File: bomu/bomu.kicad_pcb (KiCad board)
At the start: 2 copper layers, 29 parts, among them U1 NRF52840-CKAA-R7

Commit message: Current work on the PCB
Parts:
- removed TP1, TP2: TestPoint, TestPoint:TestPoint_Pad_D1.0mm
- ANT1, C1, C10, C11, C12, C13, C14, C15, C2, C3, C4, C5, C6, C7, C8, C9, L1, L2, R1, U1, XTAL1, XTAL2: moved to B.Cu
- moved C8 19.2 mm to (134.5, 133.7), turned to 90 degrees
- moved C13 18.3 mm to (133.1, 139.5), turned to 180 degrees
- moved C12 17.1 mm to (133.1, 133.7)
- moved R1 17.0 mm to (133.1, 140.3), turned to 180 degrees
- moved C15 15.9 mm to (138.9, 139.0), turned to 180 degrees
- moved C11 15.4 mm to (137.3, 133.7), turned to 270 degrees
- moved C9 14.9 mm to (135.2, 133.7), turned to 90 degrees
- moved C7 14.6 mm to (133.1, 134.4)
- moved C10 13.7 mm to (135.9, 133.7), turned to 90 degrees
- moved TP6 12.6 mm to (141.5, 133.7), turned to 90 degrees
- moved C1 12.4 mm to (142.2, 139.8), turned to 270 degrees
- moved C5 11.2 mm to (138.9, 134.8), turned to 180 degrees
- moved C6 11.1 mm to (133.1, 138.1), turned to 180 degrees
- moved L2 11.0 mm to (142.9, 139.4), turned to 180 degrees
- moved C14 10.8 mm to (137.5, 139.0)
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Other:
- board outline added: 13 x 9.4 mm
- net class Default: clearance 0.2 -> 0.0762; trace_width 0.25 -> 0.0762
- rule trace_clearance: 0.2 -> 0.0762
- rule trace_min: 0.2 -> 0.0762
- rule via_min_drill: 0.3 -> 0.2

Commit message: Changing from 2-lyaer to 4-layer
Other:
- copper layers 2 -> 4
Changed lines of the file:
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@@
 (kicad_pcb (version 20171130) (host pcbnew "(5.1.8-0-10_14)")
   (general
-    (thickness 1.6)
+    (thickness 0.8)
     (drawings 95)
     (tracks 0)
@@
   (page A4)
   (layers
-    (0 F.Cu signal)
-    (31 B.Cu signal)
+    (0 F.Cu mixed)
+    (1 In1.Cu power)
+    (2 In2.Cu power)
+    (31 B.Cu mixed)
     (32 B.Adhes user)
     (33 F.Adhes user)
@@
     (38 B.Mask user)
     (39 F.Mask user)
-    (40 Dwgs.User user hide)
+    (40 Dwgs.User user)
     (41 Cmts.User user)
     (42 Eco1.User user)

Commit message: Updating footprints. Adding SWD pads
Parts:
- added TP1: TestPoint, TestPoint:TestPoint_Pad_D1.0mm, F.Cu at (144.2, 133.9)
- moved TP3 7.87 mm to (144.2, 132.9)
- moved C1 1.18 mm to (141.1, 140.3)
- moved L1 1.18 mm to (140.4, 140.0)
- moved L2 1.18 mm to (141.8, 140.0)
- moved TP5 1.02 mm to (143.5, 132.9)
- moved TP6 0.89 mm to (141.3, 132.9)
- moved TP4 0.41 mm to (142.4, 132.9)
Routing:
- net GND: track 0.00 -> 8.57 mm, vias 0 -> 1
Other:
- copper layers 4 -> 6

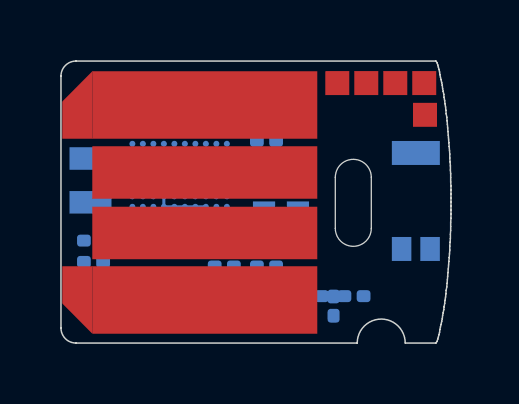
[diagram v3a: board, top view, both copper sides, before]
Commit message: Adjusting pour around antenna footprint. Adding more traces
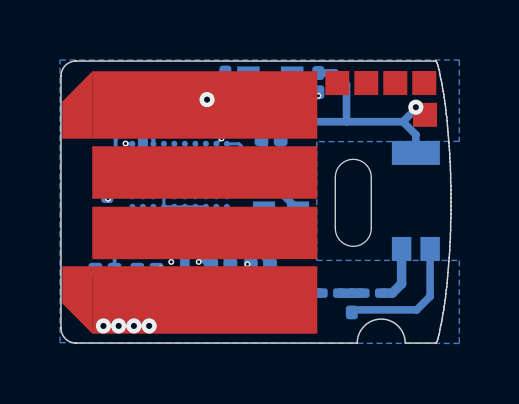
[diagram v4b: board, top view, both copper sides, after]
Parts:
- moved C6 9.16 mm to (140.6, 132.9), turned to 90 degrees
- moved XTAL2 6.75 mm to (139.0, 133.0), turned to 180 degrees
- moved C7 4.67 mm to (137.5, 132.8), turned to 270 degrees
- moved C12 2.63 mm to (133.6, 136.3), turned to 270 degrees
- moved C3 1.79 mm to (134.9, 139.1), turned to 0 degrees
- moved C15 1.53 mm to (137.4, 138.9), turned to 0 degrees
- moved C14 1.21 mm to (138.7, 138.9)
- moved C11 0.94 mm to (136.4, 133.7)
- moved C1 0.62 mm to (141.8, 140.2)
- moved L1 0.62 mm to (141.0, 139.9)
- moved L2 0.62 mm to (142.4, 139.9)
- moved C13 0.61 mm to (133.5, 139.1)
- moved C9 0.23 mm to (135.0, 133.7)
- moved C8 0.23 mm to (134.2, 133.7)
- moved C10 0.23 mm to (135.7, 133.7)
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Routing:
- net GND: track 8.57 -> 51.0 mm, vias 1 -> 9
- net +3V0: track 0.00 -> 18.5 mm, vias 0 -> 6
- net +5V: track 0.00 -> 12.1 mm, vias 0 -> 2
- net /ANT: track 0.00 -> 6.33 mm
- net /XL1: track 0.00 -> 5.83 mm, vias 0 -> 2
- net VBUS: track 0.00 -> 4.48 mm, vias 0 -> 4
- net /XL2: track 0.00 -> 2.69 mm, vias 0 -> 2
- net Net-(ANT1-PadFEED): track 0.00 -> 1.95 mm
- net Net-(C2-Pad1): track 0.00 -> 1.90 mm, vias 0 -> 2
- net Net-(C8-Pad1): track 0.00 -> 1.81 mm
- net Net-(C15-Pad2): track 0.00 -> 1.56 mm
- net Net-(C5-Pad1): track 0.00 -> 1.28 mm
- net Net-(C4-Pad2): track 0.00 -> 1.27 mm
- net Net-(C1-Pad1): track 0.00 -> 0.76 mm
- net (no net): vias 0 -> 19
- added copper zone on B.Cu, net GND

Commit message: Current work on ground planes
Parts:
- moved XTAL1 0.10 mm to (139.5, 136.5)
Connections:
- net /XL1 renamed /32XTAL_P
- net /XL2 renamed /32XTAL_N
- net Net-(C4-Pad2) renamed /XTAL_P
- net Net-(C5-Pad1) renamed /XTAL_N
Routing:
- net +3V0: track 18.5 -> 28.7 mm, vias 6 -> 7
- net /XTAL_P: track 1.27 -> 5.14 mm
- net /XTAL_N: track 1.28 -> 5.09 mm
- net /32XTAL_N: track 2.69 -> 5.15 mm
- net GND: track 51.0 -> 48.9 mm, vias 9 -> 48
- net /SWDCLK: vias 0 -> 1
- net (no net): vias 19 -> 2
- added copper zone on In4.Cu.GND, net GND

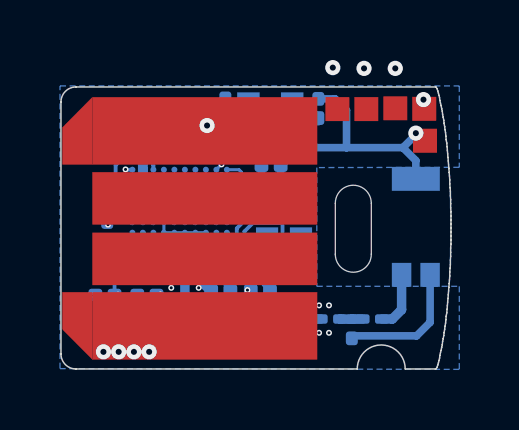
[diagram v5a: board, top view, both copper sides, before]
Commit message: Adding ground plane stitching with microvias
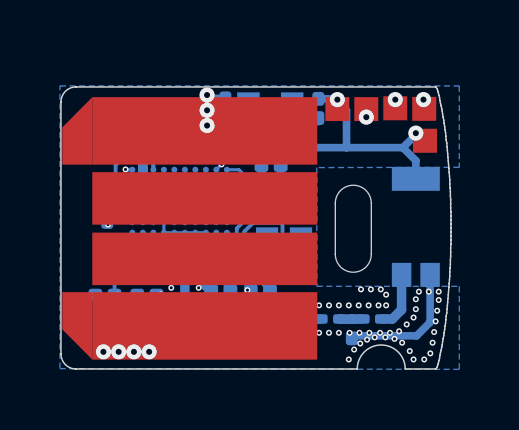
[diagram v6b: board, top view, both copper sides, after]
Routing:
- net GND: track 48.9 -> 51.2 mm, vias 48 -> 91
- net /SWDIO: vias 0 -> 1
- net /RESET: vias 0 -> 1
- net (no net): vias 2 -> 0

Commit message: Current progress on BOMU 1.0.0
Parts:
- added C_RF1: DNP, Capacitor_SMD:C_0201_0603Metric, B.Cu at (139.4, 140.6)
- added C_RF2: DNP, Capacitor_SMD:C_0201_0603Metric, B.Cu at (141.2, 140.6)
- added L3: DNP, Inductor_SMD:L_0201_0603Metric, B.Cu at (140.3, 140.3)
- added TP10: TestPoint, TestPoint:TestPoint_Pad_D1.0mm, B.Cu at (142.2, 132.9)
- added TP7: TestPoint, TestPoint:TestPoint_Pad_D1.0mm, B.Cu at (144.2, 132.9)
- added TP8: TestPoint, TestPoint:TestPoint_Pad_D1.0mm, B.Cu at (144.2, 133.9)
- added TP9: TestPoint, TestPoint:TestPoint_Pad_D1.0mm, B.Cu at (143.2, 132.9)
- moved L1 4.06 mm to (137.0, 140.3)
- moved C1 3.96 mm to (137.8, 140.6)
- moved L2 3.83 mm to (138.6, 140.3)
- moved XTAL1 0.23 mm to (139.3, 136.5)
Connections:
- net Net-(U1-PadJ8) renamed /USB_N
- net Net-(U1-PadK8) renamed /USB_P
- L2 pad 1: Net-(ANT1-PadFEED) -> Net-(C_RF1-Pad1)
- U1 pad C10: Net-(U1-PadC10) -> /P0.04
- U1 pad D10: Net-(U1-PadD10) -> /P0.05
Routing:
- net /SWDIO: track 0.00 -> 11.6 mm, vias 1 -> 2
- net /P0.04: track 0.00 -> 10.8 mm, vias 0 -> 2
- net /SWDCLK: track 0.00 -> 9.57 mm, vias 1 -> 2
- net /RESET: track 0.00 -> 9.31 mm, vias 1 -> 2
- net /P0.05: track 0.00 -> 9.13 mm, vias 0 -> 2
- net GND: track 51.2 -> 55.5 mm, vias 91 -> 327
- net /USB_P: track 0.00 -> 4.09 mm, vias 0 -> 2
- net /USB_N: track 0.00 -> 4.07 mm, vias 0 -> 2
- net /ANT: track 6.33 -> 2.64 mm
- net Net-(C15-Pad2): track 1.56 -> 4.47 mm, vias 0 -> 2
- net Net-(ANT1-PadFEED): track 1.95 -> 4.27 mm
- net Net-(C3-Pad1): track 0.00 -> 2.20 mm, vias 0 -> 2
- net Net-(C_RF1-Pad1): track 0.00 -> 1.01 mm
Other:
- rule via_min_drill: 0.2 -> 0.1
- rule via_min_size: 0.4 -> 0.2
- board text added: "1.0.0"
- board text added: "BOMU"

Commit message: Adding gerbers, and current work
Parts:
- removed C_RF2: DNP, Capacitor_SMD:C_0201_0603Metric
- removed L3: DNP, Inductor_SMD:L_0201_0603Metric
- moved C1 2.07 mm to (135.9, 139.9), turned to 180 degrees
- moved L1 1.51 mm to (136.2, 139.0), turned to 90 degrees
- moved L2 1.37 mm to (137.3, 140.3)
- moved C_RF1 1.02 mm to (138.4, 140.6)
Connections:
- C_RF1 pad 1: Net-(C_RF1-Pad1) -> Net-(ANT1-PadFEED)
- L2 pad 1: Net-(C_RF1-Pad1) -> Net-(ANT1-PadFEED)
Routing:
- net GND: track 55.5 -> 60.2 mm
- net Net-(ANT1-PadFEED): track 4.27 -> 7.30 mm
- net /ANT: track 2.64 -> 0.65 mm
- net Net-(C_RF1-Pad1): track 1.01 -> 0.00 mm
- net Net-(C1-Pad1): track 0.99 -> 1.62 mm
